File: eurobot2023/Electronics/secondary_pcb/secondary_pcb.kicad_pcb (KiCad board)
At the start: 2 copper layers, 120.9 x 93.2 mm, 34 parts, among them IC1 CD74HCT125M96, IC2 SN74LVC126ADR, J1 PI40HAT, J10 Conn_01x02_Male, J11 MagneticEncoder, J12 Conn_01x07_Male, J13 MagneticEncoder, J14 Conn_01x03_Male, J15 Conn_01x02_Male, J2 Conn_01x02_Male, J3 Conn_01x02_Male, J4 Conn_01x02_Male, J5 Conn_01x02_Male, J6 Conn_01x02_Male, J7 Conn_01x02_Male, J9 22-03-5035, P1 R-78Bxx-2.0, P2 Amazon 5A stepdown, U1 MCP2515-xSO, U2 TJA1049T, U3 PCA9306D, U4 Pololu_MAX14870, U5 PCA9685PW

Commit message: Modify secondary pcb
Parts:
- removed C3: Conn_03x08, MiAM:Pin_Header_Straight_3x08_Pitch2.54mm
- removed J14: Conn_01x03_Male, Connector_PinHeader_2.54mm:PinHeader_1x03_P2.54mm_Vertical
- removed U3: PCA9306D, Package_SO:SO-8_3.9x4.9mm_P1.27mm
- removed U5: PCA9685PW, Package_SO:TSSOP-28_4.4x9.7mm_P0.65mm
- added I2C2: Conn_01x05_Male, Connector_PinHeader_2.54mm:PinHeader_1x05_P2.54mm_Vertical, F.Cu at (71.8, 60.9)
- added I2C3: Conn_01x05_Male, Connector_PinHeader_2.54mm:PinHeader_1x05_P2.54mm_Vertical, F.Cu at (137.8, 79.4)
- added Mot V Select: Conn_01x03_Male, Connector_PinHeader_2.54mm:PinHeader_1x03_P2.54mm_Vertical, F.Cu at (103.5, 60.4)
- Enc 1: renamed from J11
- Enc 2: renamed from J13
- moved U4 65.9 mm to (109.2, 73.0), turned to 0 degrees
- moved Enc 2 53.1 mm to (135.9, 109.2)
- moved Mot 46.3 mm to (137.8, 95.9)
- moved Servo 45.4 mm to (137.8, 73.1), turned to -90 degrees
- moved CAN2 43.1 mm to (136.5, 124.5)
- moved J6 38.4 mm to (135.3, 138.4)
- moved R3 38.3 mm to (104.8, 129.3)
- moved P2 35.0 mm to (110.9, 117.8)
- moved R1 32.2 mm to (105.4, 92.7), turned to -90 degrees
- moved U2 32.2 mm to (95.2, 102.2)
- moved Enc 1 30.3 mm to (74.5, 109.2)
- moved C1 27.5 mm to (91.4, 118.0), turned to 90 degrees
- moved U1 25.2 mm to (95.9, 91.4), turned to 180 degrees
- moved R6 24.8 mm to (128.9, 60.3), turned to -90 degrees
- moved R2 24.7 mm to (117.5, 124.5)
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- renumbered J7 to CAN1, J15 to CAN2, C4 to GPIO, J12 to I2C1, J10 to Mot, J9 to Servo
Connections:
- J1 pad 33: unconnected-(J1-Pad33) -> /GPIO 13
- J1 pad 35: unconnected-(J1-Pad35) -> /GPIO 19
- U4 pad 9: +7.5V -> Net-(U4-Pad9)
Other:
- board size 120.9 x 93.2 mm -> 73.9 x 88.1 mm
- board text added: "13"
- board text added: "19"
- board text added: "Emergency"
- board text added: "ON/OFF"
- board text added: "S"
- board text added: "SCL"
- board text added: "SDA"
- board text removed: "0"
- board text removed: "1"
- board text removed: "2"
- board text removed: "3"
- board text removed: "7"
- board text removed: "A0"
- board text removed: "GPIO"
- board text removed: "I2C SCL"
- board text removed: "I2C SDA"
- board text removed: "UART RX"

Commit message: Begin routing
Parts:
- Enc1: renamed from Enc 2
- Enc2: renamed from Enc 1
- Mot V Select1: renamed from Mot V Select
- moved HC49 39.0 mm to (103.5, 78.0)
- moved C2 25.6 mm to (105.4, 94.6)
- moved C1 25.6 mm to (101.6, 94.6)
- moved U2 16.0 mm to (97.2, 118.1)
- moved U1 15.3 mm to (96.5, 106.7)
- moved R1 13.6 mm to (97.2, 81.9)
- moved J5 4.76 mm to (71.8, 134.0), turned to -90 degrees
- moved IC1 4.49 mm to (94.0, 63.5)
- moved IC2 3.86 mm to (94.0, 74.9)
- moved R3 2.21 mm to (105.4, 131.4)
- moved R2 2.01 mm to (118.1, 126.4)
- moved P2 0.64 mm to (110.5, 118.3)
- moved J3 0.19 mm to (88.8, 139.7)
- renumbered GPIO to GPIO1, Mot to Mot1, Servo to Servo1
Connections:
- IC2 pad 5: /UART_RX_5 -> /UART_HD
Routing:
- net /I2C SCL: track 0.00 -> 120.6 mm, vias 0 -> 3
- net /I2C SDA: track 0.00 -> 118.1 mm, vias 0 -> 2
- net /SPI1 CLK: track 0.00 -> 115.4 mm, vias 0 -> 3
- net Net-(CAN1-Pad2): track 0.00 -> 92.1 mm, vias 0 -> 5
- net /SPI1_CS1: track 0.00 -> 89.2 mm, vias 0 -> 2
- net Net-(CAN1-Pad1): track 0.00 -> 87.0 mm, vias 0 -> 4
- net Net-(Enc1-Pad3): track 0.00 -> 77.9 mm
- net /SPI1_CS0_5: track 0.00 -> 54.0 mm, vias 0 -> 3
- net +3.3V: track 0.00 -> 53.3 mm, vias 0 -> 1
- net /UART_TX: track 0.00 -> 52.9 mm, vias 0 -> 5
- net /SPI1 MOSI: track 0.00 -> 51.9 mm
- net /SPI1 MOSI_5: track 0.00 -> 50.6 mm, vias 0 -> 4
- net /Servo RX: track 0.00 -> 47.7 mm, vias 0 -> 2
- net /GPIO 4: track 0.00 -> 45.1 mm, vias 0 -> 1
- net /SPI1 CLK_5: track 0.00 -> 43.5 mm, vias 0 -> 2
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- added copper zone on F.Cu, net +24V
- added copper zone on F.Cu, net Net-(J2-Pad2)

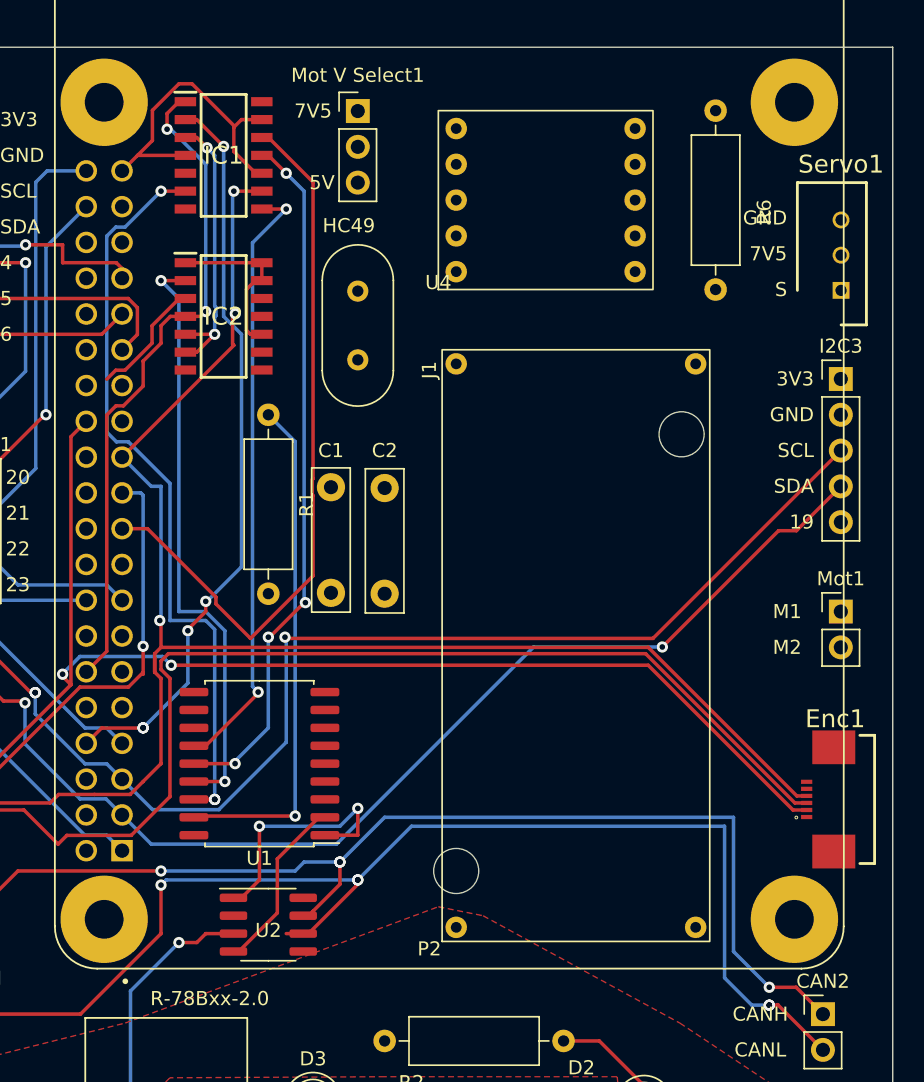
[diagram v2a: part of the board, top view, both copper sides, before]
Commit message: Update PCB routing
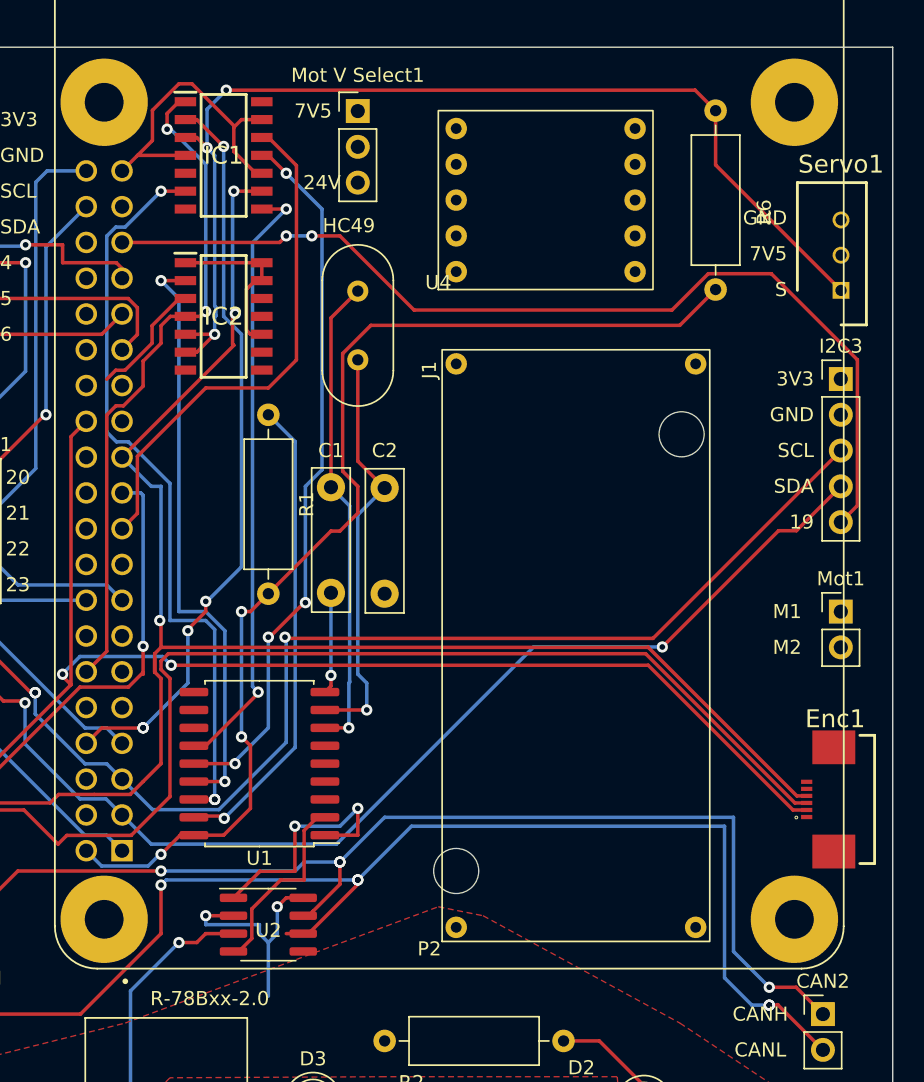
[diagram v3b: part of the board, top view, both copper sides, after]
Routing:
- net +5V: track 17.4 -> 96.9 mm, vias 1 -> 4
- net /GPIO 19: track 0.00 -> 70.2 mm, vias 0 -> 2
- net /UART_HD: track 20.1 -> 76.8 mm, vias 2 -> 3
- net Net-(C1-Pad2): track 0.00 -> 34.1 mm, vias 0 -> 1
- net Net-(C2-Pad2): track 0.00 -> 29.7 mm, vias 0 -> 1
- net GND: track 24.1 -> 48.1 mm, vias 0 -> 3
- net /SPI1 MOSI: track 51.9 -> 36.8 mm
- net Net-(R1-Pad1): track 37.1 -> 34.3 mm
- net Net-(U1-Pad2): track 12.7 -> 13.7 mm
- net /SPI1 MOSI_5: track 50.6 -> 51.6 mm
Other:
- board text added: "24V"
- board text removed: "5V"

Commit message: Update secondary pcb routing
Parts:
- moved Mot1 28.6 mm to (137.2, 67.3)
- moved Mot V Select1 22.8 mm to (122.0, 73.7), turned to -90 degrees
- moved Servo1 10.1 mm to (137.2, 83.2)
- moved I2C3 10.1 mm to (136.5, 89.4)
- moved U4 3.18 mm to (109.2, 69.8)
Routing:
- net +3.3V: track 53.3 -> 182.9 mm, vias 1 -> 8
- net +24V: track 0.00 -> 57.1 mm
- net +5V: track 96.9 -> 143.1 mm, vias 4 -> 6
- net /GPIO 12: track 0.00 -> 41.1 mm, vias 0 -> 1
- net /GPIO 16: track 0.00 -> 30.4 mm
- net /SPI1_CS0: track 0.00 -> 29.9 mm, vias 0 -> 1
- net /UART_HD: track 76.8 -> 95.3 mm, vias 3 -> 5
- net Net-(Mot1-Pad1): track 0.00 -> 16.6 mm
- net Net-(Mot1-Pad2): track 0.00 -> 16.6 mm
- net /GPIO 19: track 70.2 -> 83.7 mm
- net Net-(Mot V Select1-Pad2): track 0.00 -> 9.17 mm
- net /SPI1 MISO: track 39.9 -> 47.2 mm, vias 1 -> 4
- net Net-(CAN1-Pad2): track 92.1 -> 85.4 mm, vias 5 -> 4
- net Net-(CAN1-Pad1): track 87.0 -> 80.7 mm, vias 4 -> 5
- net /I2C SCL: track 120.6 -> 115.5 mm, vias 3 -> 5
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- added copper zone on F.Cu, net +7.5V
- added copper zone on B.Cu, net GND

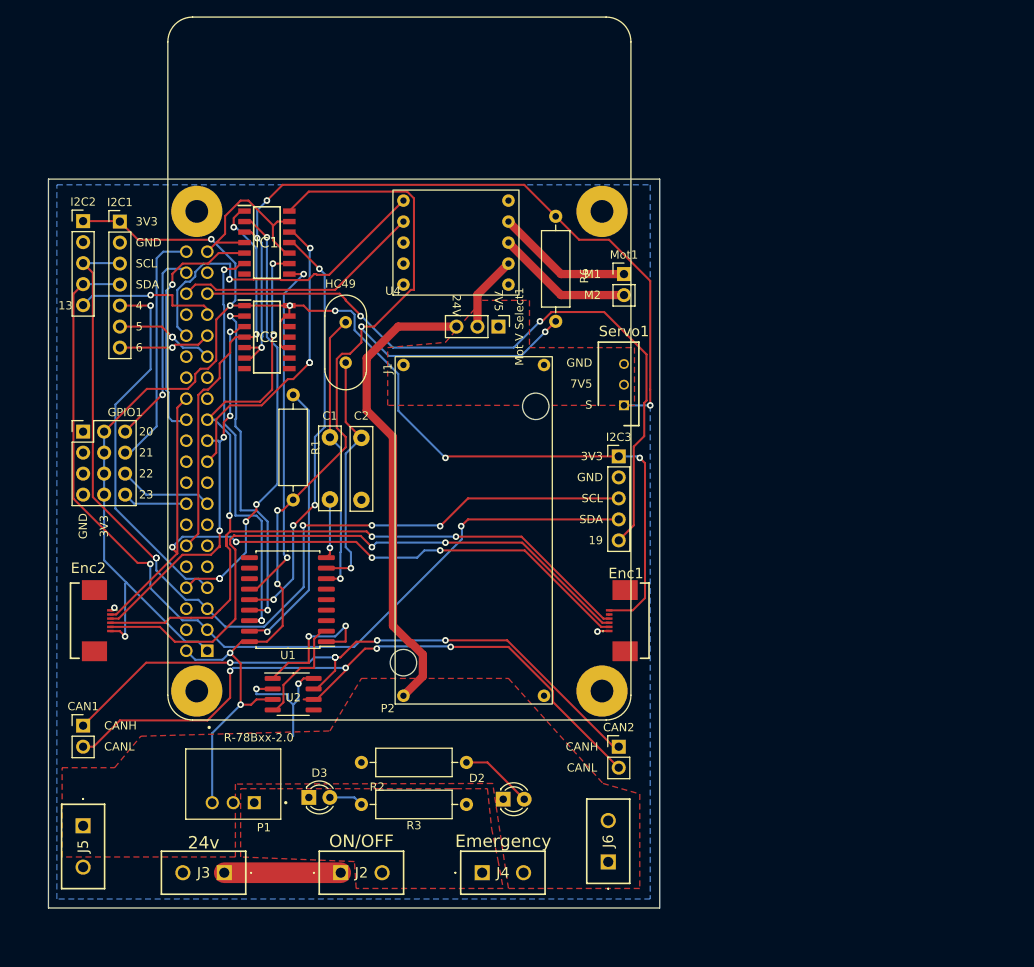
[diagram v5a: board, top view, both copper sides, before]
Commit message: Electronics: correct PCB schematic and component references.
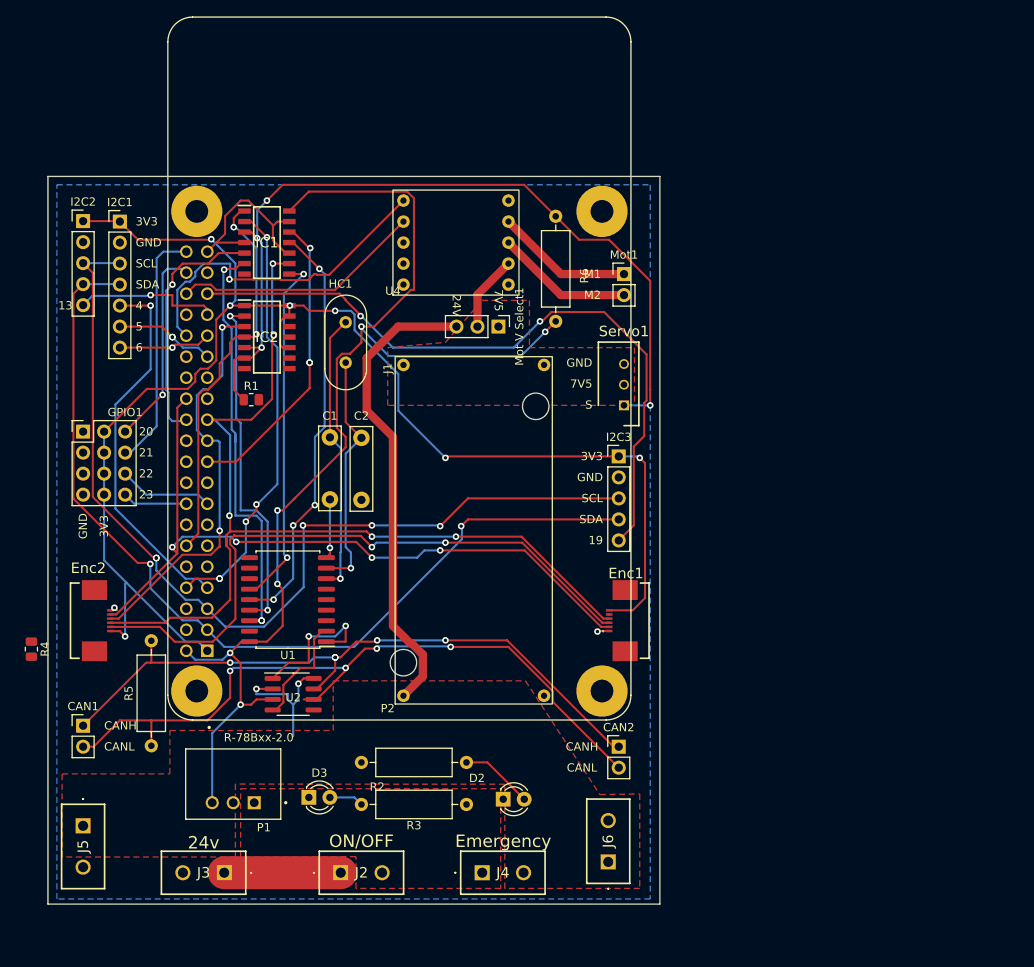
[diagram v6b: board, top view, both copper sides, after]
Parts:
- added R4: 10k, Resistor_SMD:R_0805_2012Metric, F.Cu at (65.5, 112.7)
- added R5: 120, Resistor_THT:R_Axial_DIN0309_L9.0mm_D3.2mm_P12.70mm_Horizontal, F.Cu at (80.0, 124.3)
- R1: footprint Resistor_THT:R_Axial_DIN0309_L9.0mm_D3.2mm_P12.70mm_Horizontal -> Resistor_SMD:R_0805_2012Metric
- moved R1 5.10 mm to (92.1, 82.5), turned to 0 degrees
- renumbered HC49 to HC1
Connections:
- net /Servo RX renamed /Servo DIR
- I2C2 pad 5: /GPIO 13 -> /GPIO 17
- I2C3 pad 5: /GPIO 19 -> /GPIO 27
- IC1 pad 3: /UART_HD -> /UART_HalfDuplex
- IC2 pad 5: /UART_HD -> /UART_HalfDuplex
- IC2 pad 6: /UART_HD -> /UART_RX
- J1 pad 11: unconnected-(J1-Pad11) -> /GPIO 17
- J1 pad 13: unconnected-(J1-Pad13) -> /GPIO 27
- R1 pad 1: Net-(R1-Pad1) -> /UART_RX
- R6 pad 1: /UART_HD -> /UART_HalfDuplex
- Servo1 pad 1: /UART_HD -> /UART_HalfDuplex
- U1 pad 17: Net-(R1-Pad1) -> Net-(R4-Pad1)
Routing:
- net /UART_HD: track 95.3 -> 0.00 mm, vias 5 -> 0
- net /UART_HalfDuplex: track 0.00 -> 94.5 mm, vias 0 -> 5
- net Net-(R1-Pad1): track 34.3 -> 0.00 mm, vias 1 -> 0
- net /GPIO 17: track 0.00 -> 17.6 mm, vias 0 -> 1
- net /GPIO 13: track 17.6 -> 0.00 mm, vias 1 -> 0
- net /UART_RX: track 0.00 -> 6.62 mm
- net Net-(CAN1-Pad2): track 85.4 -> 88.4 mm
- net Net-(CAN1-Pad1): track 80.7 -> 83.3 mm
- net /SPI1 MISO: track 47.2 -> 49.9 mm, vias 4 -> 2
- net /SPI1_CS0_5: track 50.6 -> 51.4 mm
- net Net-(R4-Pad1): track 0.00 -> 0.68 mm
- net /SPI1 CLK: track 117.9 -> 118.5 mm
- net /SPI1 MOSI: track 37.0 -> 36.4 mm
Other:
- board size 73.9 x 88.1 mm -> 74 x 88 mm

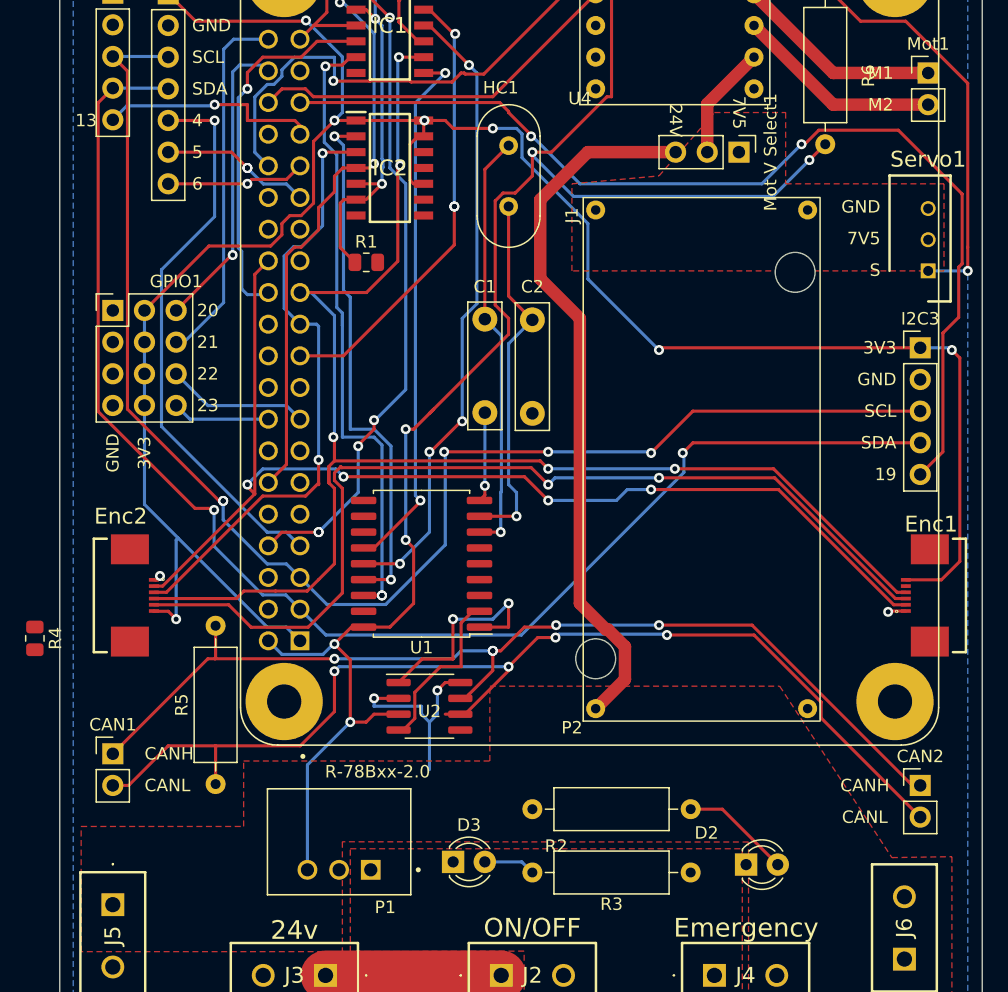
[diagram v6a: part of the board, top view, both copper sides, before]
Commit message: Electronics: update PCB
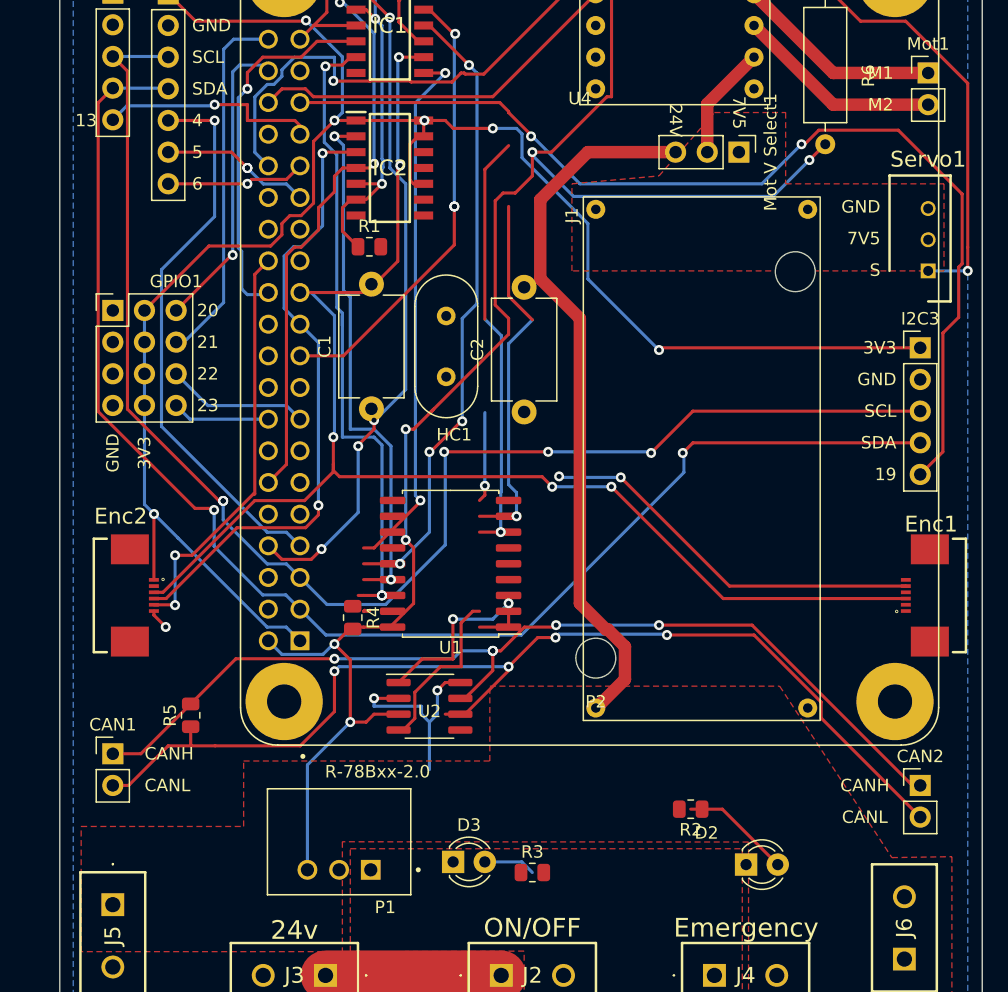
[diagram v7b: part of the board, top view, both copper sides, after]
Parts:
- C1, C2: footprint Capacitor_THT:C_Rect_L10.0mm_W2.5mm_P7.50mm_MKS4 -> Capacitor_THT:C_Disc_D8.0mm_W5.0mm_P10.00mm
- R2, R3, R5: footprint Resistor_THT:R_Axial_DIN0309_L9.0mm_D3.2mm_P12.70mm_Horizontal -> Resistor_SMD:R_0805_2012Metric
- moved R4 25.6 mm to (91.0, 111.0)
- moved HC1 10.1 mm to (98.5, 86.8), turned to -90 degrees
- moved C1 9.11 mm to (92.5, 94.2)
- moved R5 5.86 mm to (78.0, 118.8)
- moved U1 2.33 mm to (98.8, 106.7)
- moved R1 1.27 mm to (92.3, 81.2)
- moved C2 0.67 mm to (104.8, 94.5)
- moved P2 0.05 mm to (110.5, 118.2)
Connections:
- Enc1 pad 1: GND -> +3.3V
- Enc1 pad 2: /SPI1_CS1 -> unconnected-(Enc1-Pad2)
- Enc1 pad 3: Net-(Enc1-Pad3) -> /SPI1 CLK
- Enc1 pad 4: /SPI1 CLK -> Net-(Enc1-Pad4)
- Enc1 pad 5: unconnected-(Enc1-Pad5) -> /SPI1_CS1
- Enc1 pad 6: +3.3V -> GND
- Enc2 pad 1: GND -> +3.3V
- Enc2 pad 2: /SPI1_CS1 -> Net-(Enc1-Pad4)
- Enc2 pad 3: /SPI1 MISO -> /SPI1 CLK
- Enc2 pad 4: /SPI1 CLK -> /SPI1 MISO
- Enc2 pad 5: Net-(Enc1-Pad3) -> /SPI1_CS1
- Enc2 pad 6: +3.3V -> GND
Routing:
- net Net-(Enc1-Pad3): track 77.8 -> 0.00 mm, vias 2 -> 0
- net Net-(C2-Pad2): track 29.7 -> 86.8 mm
- net +24V: track 57.1 -> 0.00 mm
- net +5V: track 143.6 -> 187.1 mm, vias 6 -> 8
- net /SPI1 CLK_5: track 43.5 -> 0.00 mm, vias 2 -> 0
- net +3.3V: track 182.9 -> 154.8 mm, vias 8 -> 7
- net /SPI1_CS1: track 89.9 -> 64.9 mm
- net Net-(U1-Pad1): track 17.6 -> 0.00 mm, vias 2 -> 0
- net Net-(CAN1-Pad1): track 83.3 -> 98.2 mm, vias 5 -> 7
- net /UART_RX: track 6.62 -> 0.00 mm
- net /SPI1 CLK: track 118.5 -> 113.1 mm
- net /UART_HalfDuplex: track 94.5 -> 99.5 mm
- net /UART_TX: track 52.9 -> 54.7 mm, vias 5 -> 4
- net Net-(CAN1-Pad2): track 88.4 -> 86.9 mm
- net /SPI1 MISO: track 49.9 -> 50.5 mm
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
